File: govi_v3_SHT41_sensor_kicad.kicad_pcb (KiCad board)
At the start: 2 copper layers, 83 x 108 mm, 72 parts, among them J201 2.54mm 4-Pin JST, J202 Conn_01x04, J401 7.62mm 2-Pin Screw Terminal, J501 7.62mm 2-Pin Screw Terminal, J502 Conn_02x02_Odd_Even, Q501 Q_PMOS_Depletion, Q701 FS8205A, SW201 SW_Push, U201 STM32F103C6Tx, U301 Ra-02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

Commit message: "PCB front Layer Component assembly done"
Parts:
- removed C402: 0.1MFD/16V, Capacitor_SMD:C_0603_1608Metric_Pad1.08x0.95mm_HandSolder
- removed C403: 10MFD/16V, Capacitor_SMD:C_0603_1608Metric_Pad1.08x0.95mm_HandSolder
- removed J502: Conn_02x02_Odd_Even, Connector_PinHeader_2.54mm:PinHeader_2x02_P2.54mm_Vertical
- removed R505: R040 40mΩ, Resistor_SMD:R_2512_6332Metric_Pad1.40x3.35mm_HandSolder
- added G***: LOGO, govi_v3_SHT41_sensor_kicad:govi-ai-logo-front, F.Cu at (231.0, 99.0)
- added J203: Conn_01x04, Connector_PinHeader_2.54mm:PinHeader_1x04_P2.54mm_Vertical, F.Cu at (192.2, 126.0)
- added R207: 10K, Resistor_SMD:R_0402_1005Metric_Pad0.72x0.64mm_HandSolder, F.Cu at (165.2, 118.2)
- added R208: 10K, Resistor_SMD:R_0402_1005Metric_Pad0.72x0.64mm_HandSolder, F.Cu at (182.3, 92.3)
- added TP401: 5V, TestPoint:TestPoint_Pad_D1.0mm, F.Cu at (187.9, 91.7)
- added TP501: MPPT, TestPoint:TestPoint_Pad_D1.0mm, F.Cu at (230.3, 115.8)
- added TP601: 4056, TestPoint:TestPoint_Pad_D1.0mm, F.Cu at (191.5, 102.9)
- added TP701: BAT-, TestPoint:TestPoint_Pad_D1.0mm, F.Cu at (230.3, 118.7)
- added TP801: 3.3V, TestPoint:TestPoint_Pad_D1.0mm, F.Cu at (199.3, 115.8)
- C501, C502, C503, C504, C505, C506, C507, C701, C702, D501, D502, D503, L501, Q501, Q701, R501, R502, R503, R701, R702, U501, U701: moved to B.Cu
- J201: value 2.54mm 4-Pin JST -> Conn_01x03; footprint Connector_JST:JST_EH_B4B-EH-A_1x04_P2.50mm_Vertical -> Connector_PinHeader_2.54mm:PinHeader_1x03_P2.54mm_Vertical
- J202: value Conn_01x04 -> 2.54mm 4-Pin JST; footprint Connector_PinHeader_2.54mm:PinHeader_1x04_P2.54mm_Vertical -> Connector_JST:JST_EH_B4B-EH-A_1x04_P2.50mm_Vertical
- R204: value 1K -> 10K
- R205: value 10K -> 1K
- R504: value 36K -> R040 40mΩ; footprint Resistor_SMD:R_0603_1608Metric_Pad0.98x0.95mm_HandSolder -> Resistor_SMD:R_2512_6332Metric_Pad1.40x3.35mm_HandSolder; moved to B.Cu
- SW201: footprint Button_Switch_THT:SW_Tactile_SPST_Angled_PTS645Vx31-2LFS -> Connector_PinHeader_2.54mm:PinHeader_1x02_P2.54mm_Vertical
- moved J401 416.8 mm to (190.5, 46.9), turned to 180 degrees
- moved TH401 411.9 mm to (195.4, 54.3), turned to -90 degrees
- moved RV401 406.6 mm to (186.7, 60.3), turned to 90 degrees
- moved FL401 396.0 mm to (178.8, 53.1), turned to 180 degrees
- moved D601 390.3 mm to (198.2, 101.0), turned to 180 degrees
- moved U601 389.9 mm to (197.8, 95.4)
- moved R504 378.2 mm to (231.0, 94.2), turned to -90 degrees
- moved C601 378.1 mm to (192.3, 97.2), turned to 90 degrees
- moved PS401 377.8 mm to (162.1, 72.9)
- moved R601 377.1 mm to (192.3, 93.6), turned to -90 degrees
- moved J501 369.2 mm to (230.2, 61.2), turned to 90 degrees
- moved R503 356.3 mm to (208.2, 70.3)
- moved R502 356.0 mm to (208.2, 72.8)
- moved R501 355.7 mm to (208.2, 75.3)
- moved D503 355.5 mm to (229.2, 77.7)
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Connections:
- J201 pad 1: +3V3 -> /MCU/USART1_RX
- J201 pad 2: /MCU/I2C1_SDA -> /MCU/USART1_TX
- J201 pad 3: /MCU/I2C1_SCL -> GND
- J202 pad 2: /MCU/SWDIO -> /MCU/I2C1_SDA
- J202 pad 3: /MCU/SWCLK -> /MCU/I2C1_SCL
- R202 pad 1: /MCU/BOOT0 -> +3V3
- R202 pad 2: GND -> /MCU/I2C1_SCL
- R203 pad 1: Net-(R201-Pad2) -> /MCU/BOOT0
- R203 pad 2: /MCU/PAIR_BTN -> GND
- R204 pad 1: Net-(D201-A) -> Net-(R201-Pad2)
- R204 pad 2: +3V3 -> /MCU/PAIR_BTN
- R205 pad 1: /MCU/LoRa_INT -> Net-(D201-A)
- R205 pad 2: GND -> +3V3
- R206 pad 2: /MCU/RESET -> /MCU/I2C1_SDA
- R502 pad 1: Net-(J502-Pin_1) -> +12V
- R504 pad 1: Net-(J502-Pin_3) -> Net-(U501-CSP)
- R504 pad 2: Net-(U501-MPPT) -> Net-(D503-A)
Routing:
- net +3V3: track 0.00 -> 9.09 mm
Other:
- board size 83 x 108 mm -> 81 x 89 mm
- board text added: "+"
- board text added: "-"
- board text added: "230VAC"
- board text added: "3"
- board text added: "4056"
- board text added: "5"
- board text added: "B-"
- board text added: "L"
- board text added: "M"
- board text added: "N"
- board text added: "SOLAR 12V"
- board text added: "Temperature & Humidity Sensor v1.0"

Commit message: "Working on Routing MCU"
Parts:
- removed D501: SS54, Diode_SMD:D_SMA
- moved C501 30.3 mm to (217.7, 59.1), turned to 90 degrees
- moved C502 29.0 mm to (220.4, 59.1), turned to 90 degrees
- moved D503 25.3 mm to (204.0, 79.6), turned to 90 degrees
- moved R504 21.9 mm to (210.5, 86.4), turned to 180 degrees
- moved R702 20.7 mm to (217.8, 115.8), turned to 180 degrees
- moved R701 18.0 mm to (208.4, 115.8), turned to 180 degrees
- moved C702 17.4 mm to (213.1, 118.2), turned to 180 degrees
- moved C504 16.7 mm to (219.3, 70.4), turned to 180 degrees
- moved L501 15.3 mm to (215.4, 97.1), turned to 90 degrees
- moved U501 13.6 mm to (216.5, 76.3), turned to -90 degrees
- moved C204 13.6 mm to (169.0, 103.8), turned to 180 degrees
- moved U701 13.2 mm to (217.5, 110.8)
- moved Q701 12.9 mm to (210.1, 110.9), turned to 180 degrees
- moved C505 12.9 mm to (210.6, 67.7)
- moved C701 12.5 mm to (213.1, 115.8), turned to 180 degrees
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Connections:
- D502 pad 1: Net-(D501-K) -> Net-(D502-K)
- L501 pad 1: Net-(D501-K) -> Net-(D502-K)
- Q501 pad 1: (no net) -> Net-(Q501-G)
- Q501 pad 2: (no net) -> Net-(D502-K)
- Q501 pad 3: (no net) -> +12V
- U501 pad 10: Net-(U501-DRV) -> Net-(Q501-G)
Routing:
- net Net-(C401-Pad1): track 0.00 -> 34.7 mm
- net +3V3: track 9.09 -> 42.6 mm, vias 0 -> 5
- net /MCU/LED: track 0.00 -> 32.9 mm, vias 0 -> 1
- net Net-(PS401-AC/N): track 0.00 -> 28.0 mm
- net Net-(J401-Pin_1): track 0.00 -> 21.5 mm
- net /MCU/OSC_OUT: track 0.00 -> 18.8 mm
- net Net-(PS401-AC/L): track 0.00 -> 18.5 mm
- net /LoRa_Module_Ra-02/LoRa-NSS: track 0.00 -> 16.6 mm
- net /MCU/OSC_IN: track 0.00 -> 14.9 mm
- net +3.3VA: track 0.00 -> 14.2 mm
- net /LoRa_Module_Ra-02/LoRa-SCK: track 0.00 -> 11.9 mm
- net /MCU/RESET: track 0.00 -> 11.5 mm, vias 0 -> 2
- net /MCU/BOOT0: track 0.00 -> 9.54 mm, vias 0 -> 2
- net Net-(R201-Pad2): track 0.00 -> 7.91 mm
- net Net-(D201-A): track 0.00 -> 7.90 mm
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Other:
- outline, holes or cut-outs redrawn
- board text added: "Temperature & Humidity Sensor"
- board text added: "V1.0"
- board text removed: "Temperature & Humidity Sensor v1.0"

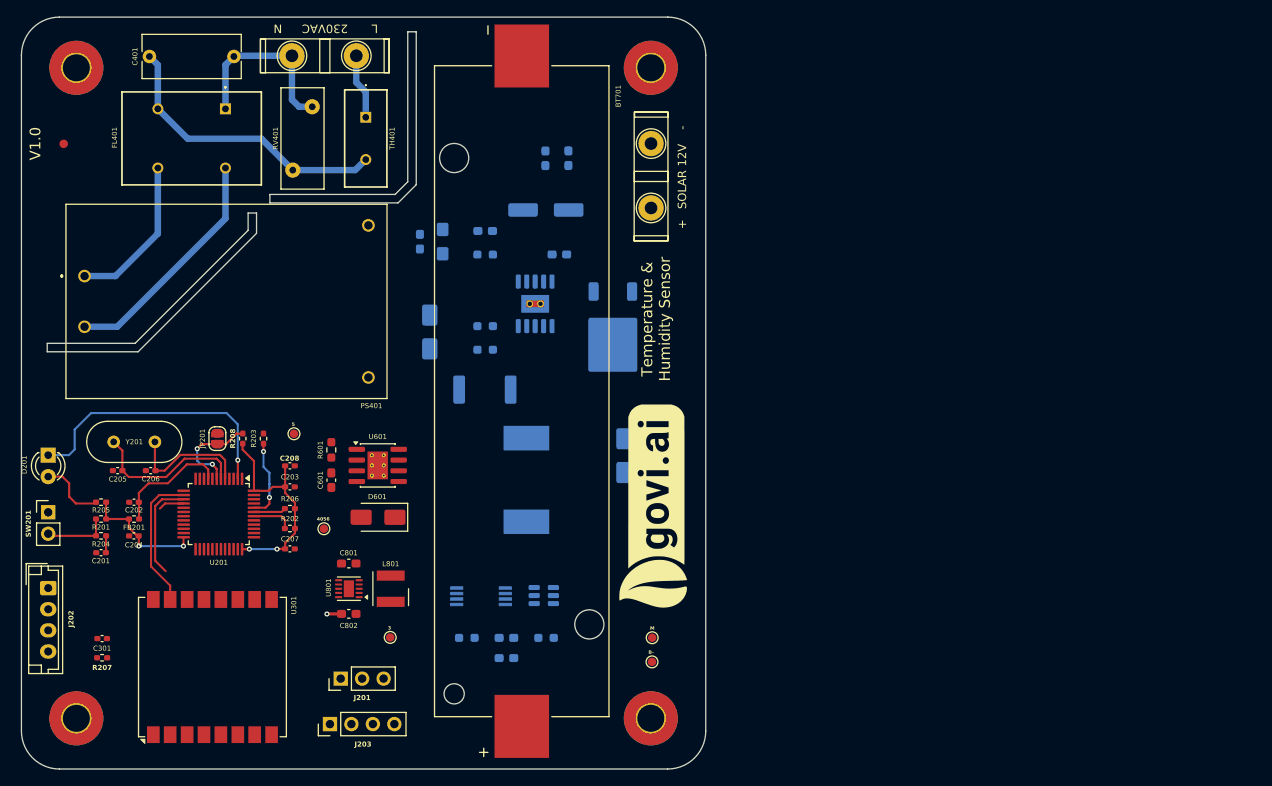
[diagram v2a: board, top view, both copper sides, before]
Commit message: "Before changing the orientation of the LoRa module. removing existing LoRa module routing."
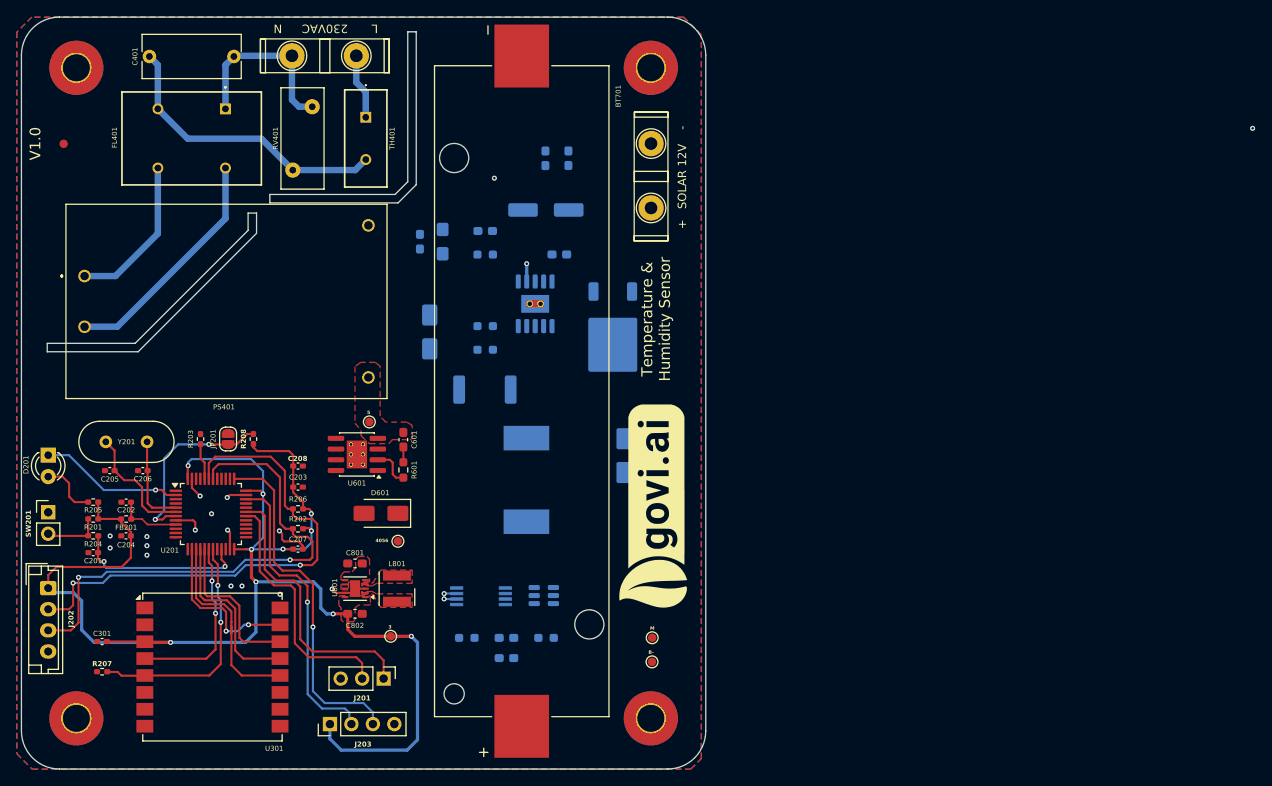
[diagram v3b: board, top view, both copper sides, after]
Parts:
- moved C601 9.78 mm to (200.9, 92.4), turned to -90 degrees
- moved TP401 9.03 mm to (196.8, 90.3)
- moved TP601 8.88 mm to (200.2, 104.4)
- moved R601 8.85 mm to (200.9, 96.0), turned to 90 degrees
- moved R203 7.46 mm to (176.9, 92.3)
- moved J201 5.08 mm to (198.5, 120.7), turned to -90 degrees
- moved U601 2.79 mm to (195.4, 94.1), turned to 180 degrees
- moved R207 1.65 mm to (165.2, 119.8)
- moved JP201 1.27 mm to (180.1, 92.3)
- moved R208 1.27 mm to (183.1, 92.3)
- moved C203 0.96 mm to (188.4, 98.0)
- moved C207 0.96 mm to (188.4, 105.3)
- moved C208 0.96 mm to (188.4, 95.5)
- moved R202 0.96 mm to (188.4, 102.9)
- moved R206 0.96 mm to (188.4, 100.6)
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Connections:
- H101 pad 1: GND -> unconnected-(H101-Pad1)_1
- TP501 pad 1: /3.3v_BuckBoost/IN+ -> Net-(D503-A)
- TP601 pad 1: /3.3v_BuckBoost/IN+ -> Net-(D601-A)
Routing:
- net +3V3: track 42.6 -> 173.1 mm, vias 5 -> 10
- net /MCU/I2C1_SDA: track 3.82 -> 61.2 mm, vias 0 -> 2
- net /MCU/I2C1_SCL: track 4.86 -> 60.4 mm, vias 0 -> 2
- net /MCU/SWCLK: track 0.00 -> 41.7 mm, vias 0 -> 1
- net /MCU/SWDIO: track 0.00 -> 35.8 mm, vias 0 -> 1
- net /MCU/USART1_RX: track 0.00 -> 33.1 mm
- net /MCU/USART1_TX: track 0.00 -> 30.0 mm
- net /MCU/LoRa_INT: track 0.00 -> 28.2 mm, vias 0 -> 2
- net GND: track 0.07 -> 26.1 mm, vias 0 -> 19
- net /LoRa_Module_Ra-02/LoRa-RESET: track 0.00 -> 21.0 mm, vias 0 -> 2
- net /MCU/PAIR_BTN: track 2.17 -> 21.0 mm, vias 0 -> 2
- net /LoRa_Module_Ra-02/LoRa-MOSI: track 0.00 -> 18.8 mm
- net /LoRa_Module_Ra-02/LoRa-MISO: track 3.07 -> 20.9 mm
- net /MCU/LED: track 32.9 -> 17.1 mm
- net /LoRa_Module_Ra-02/LoRa-SCK: track 11.9 -> 23.2 mm
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- added copper zone on F.Cu, net +3V3
- added copper zone on F.Cu, net +5V
- added copper zone on F.Cu, net /3.3v_BuckBoost/IN+
- added copper zone on B.Cu, net GND
- added copper zone on F.Cu, net GND
- added copper zone on F.Cu, net Net-(U801-L1)
- added copper zone on F.Cu, net Net-(U801-L2)

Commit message: "Routing done. DRC pending"
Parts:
- U501: footprint Package_SO:SSOP-10-1EP_3.9x4.9mm_P1mm_EP2.1x3.3mm_ThermalVias -> Package_SO:SSOP-10_3.9x4.9mm_P1.00mm
- moved H104 125.7 mm to (104.8, 134.3), turned to -90 degrees
- moved TP701 119.9 mm to (111.4, 134.5), turned to -90 degrees
- moved TP501 117.5 mm to (114.3, 134.5), turned to -90 degrees
- moved C502 110.5 mm to (136.1, 130.4), turned to -90 degrees
- moved G*** 107.3 mm to (129.5, 135.0), turned to 0 degrees
- moved C501 106.4 mm to (138.8, 130.4), turned to -90 degrees
- moved R702 103.4 mm to (114.3, 118.2), turned to 90 degrees
- moved C702 102.1 mm to (111.1, 114.4)
- moved C503 99.8 mm to (136.8, 123.6), turned to 90 degrees
- moved C701 98.8 mm to (114.3, 113.5), turned to 90 degrees
- moved H102 98.7 mm to (181.8, 134.3), turned to -90 degrees
- moved U701 97.3 mm to (120.3, 114.0), turned to 90 degrees
- moved J501 95.4 mm to (169.0, 134.4), turned to 0 degrees
- moved R701 94.3 mm to (114.3, 122.9), turned to -90 degrees
- moved J203 93.0 mm to (104.1, 96.3), turned to 0 degrees
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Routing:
- net Net-(BT701--): track 0.00 -> 107.1 mm, vias 0 -> 1
- net /3.3v_BuckBoost/IN+: track 0.52 -> 66.4 mm, vias 0 -> 3
- net Net-(D503-A): track 0.00 -> 63.0 mm, vias 0 -> 1
- net +12V: track 0.00 -> 38.5 mm
- net +5V: track 0.00 -> 31.8 mm
- net Net-(U701-CS): track 0.00 -> 14.1 mm
- net Net-(U701-OD): track 0.00 -> 13.0 mm
- net Net-(U701-VCC): track 0.00 -> 12.6 mm
- net Net-(Q501-G): track 0.00 -> 10.7 mm
- net /LoRa_Module_Ra-02/LoRa-NSS: track 19.6 -> 29.0 mm, vias 2 -> 0
- net Net-(U501-CSP): track 0.00 -> 8.39 mm
- net Net-(D601-A): track 0.21 -> 6.76 mm
- net /MCU/LoRa_INT: track 28.2 -> 22.6 mm, vias 2 -> 0
- net /LoRa_Module_Ra-02/LoRa-MOSI: track 18.8 -> 24.2 mm
- net Net-(U501-MPPT): track 0.00 -> 5.01 mm
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- added copper zone on B.Cu, net +12V
- added copper zone on B.Cu, net +3V3
- added copper zone on B.Cu, net Net-(D502-K)
- added copper zone on B.Cu, net Net-(D503-A)
- added copper zone on B.Cu, net Net-(U501-CSP)
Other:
- board size 81 x 89 mm -> 89 x 81 mm
